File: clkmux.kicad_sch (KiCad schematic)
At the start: 9 parts, among them J7 Conn_Coaxial, U3 9DMV0141AKILF, U4 DS90C401M_NOPB

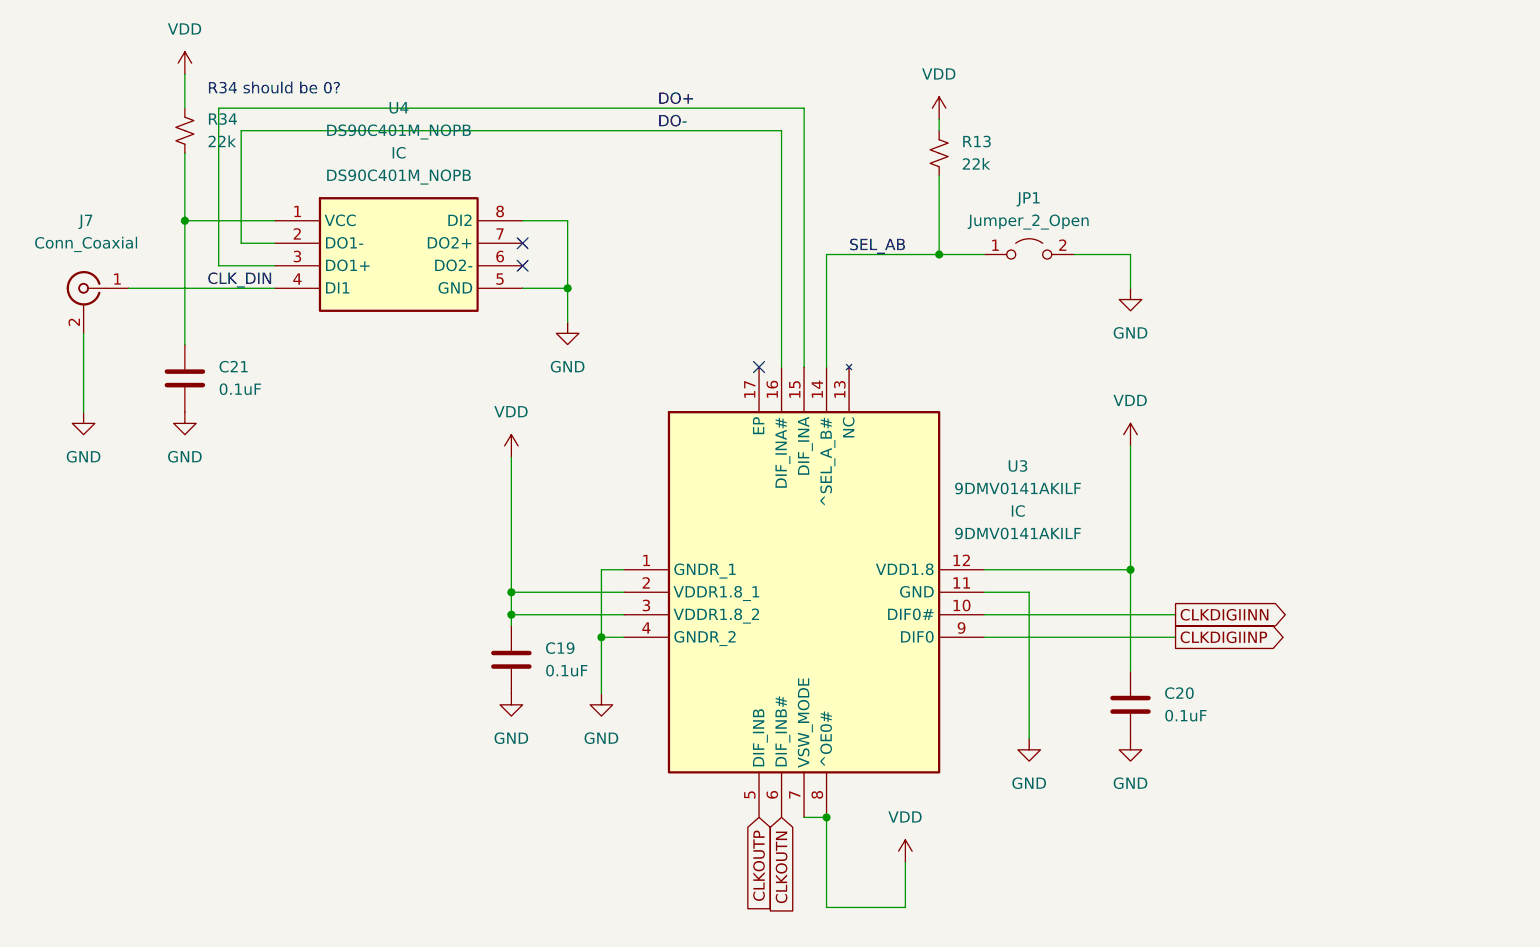
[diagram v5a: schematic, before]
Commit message: clk select related components moved to the top layer
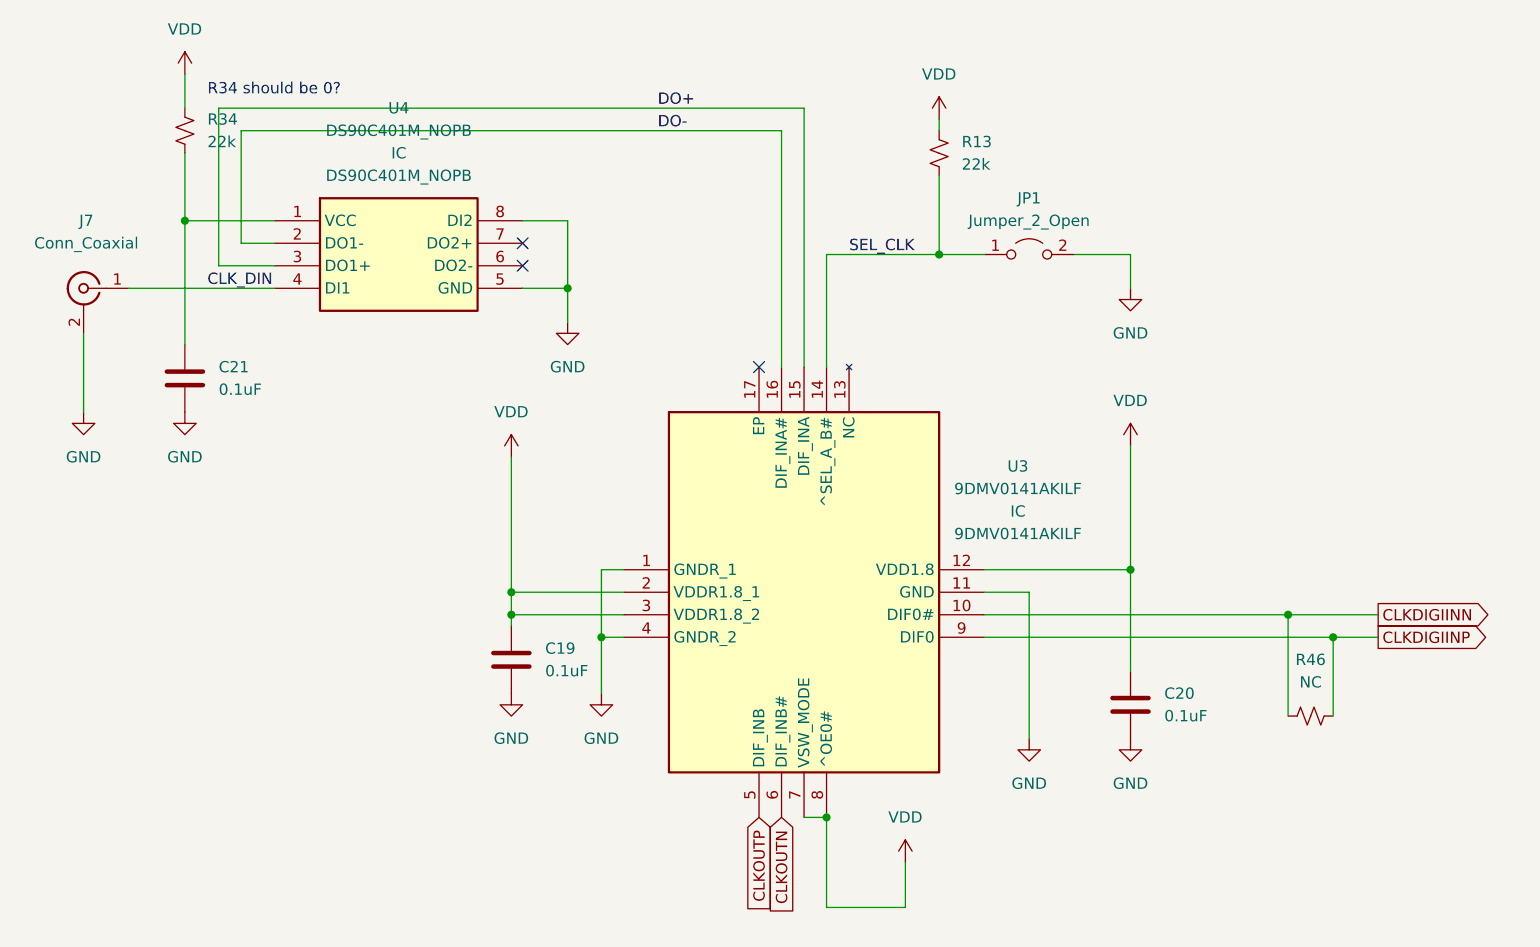
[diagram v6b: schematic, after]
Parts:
- added R46: NC, Resistor_SMD:R_0805_2012Metric_Pad1.20x1.40mm_HandSolder, symbol Device:R_Small_US
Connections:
- net CLKDIGIINN: now also R46.1
- net CLKDIGIINP: now also R46.2
- net SEL_AB renamed SEL_CLK
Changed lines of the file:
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@@
   (junction (at 71.12 72.39) (diameter 0) (color 0 0 0 0)
   )
+  (junction (at 195.58 116.84) (diameter 0) (color 0 0 0 0)
+  )
   (junction (at 156.21 76.2) (diameter 0) (color 0 0 0 0)
+  )
+  (junction (at 200.66 119.38) (diameter 0) (color 0 0 0 0)
   )
   (junction (at 177.8 111.76) (diameter 0) (color 0 0 0 0)
@@
     (stroke (width 0) (type default))
   )
+  (wire (pts (xy 200.66 119.38) (xy 161.29 119.38))
+    (stroke (width 0) (type default))
+  )
   (wire (pts (xy 177.8 111.76) (xy 177.8 123.19))
     (stroke (width 0) (type default))
@@
     (stroke (width 0) (type default))
   )
-  (wire (pts (xy 182.88 119.38) (xy 161.29 119.38))
+  (wire (pts (xy 205.74 119.38) (xy 200.66 119.38))
     (stroke (width 0) (type default))
   )
@@
     (stroke (width 0) (type default))
   )
+  (wire (pts (xy 195.58 116.84) (xy 161.29 116.84))
+    (stroke (width 0) (type default))
+  )
   (wire (pts (xy 143.51 139.7) (xy 143.51 149.86))
     (stroke (width 0) (type default))
@@
     (stroke (width 0) (type default))
   )
+  (wire (pts (xy 200.66 119.38) (xy 200.66 128.27))
+    (stroke (width 0) (type default))
+  )
   (wire (pts (xy 156.21 60.96) (xy 156.21 62.23))
     (stroke (width 0) (type default))
   )
+  (wire (pts (xy 195.58 116.84) (xy 195.58 128.27))
+    (stroke (width 0) (type default))
+  )
   (wire (pts (xy 161.29 114.3) (xy 166.37 114.3))
     (stroke (width 0) (type default))
@@
     (stroke (width 0) (type default))
   )
-  (wire (pts (xy 182.88 116.84) (xy 161.29 116.84))
+  (wire (pts (xy 205.74 116.84) (xy 195.58 116.84))
     (stroke (width 0) (type default))
   )
@@
     (effects (font (size 1.27 1.27)) (justify left bottom))
   )
-  (label "SEL_AB" (at 146.05 76.2 0) (fields_autoplaced)
+  (label "SEL_CLK" (at 146.05 76.2 0) (fields_autoplaced)
     (effects (font (size 1.27 1.27)) (justify left bottom))
   )
@@
     )
   )
-  (global_label "CLKDIGIINN" (shape output) (at 182.88 116.84 0) (fields_autoplaced)
+  (global_label "CLKDIGIINN" (shape output) (at 205.74 116.84 0) (fields_autoplaced)
     (effects (font (size 1.27 1.27)) (justify left))
-    (property "Intersheetrefs" "${INTERSHEET_REFS}" (at 195.8764 116.7606 0)
+    (property "Intersheetrefs" "${INTERSHEET_REFS}" (at 218.7364 116.7606 0)
       (effects (font (size 1.27 1.27)) (justify left) hide)
     )
@@
     )
   )
-  (global_label "CLKDIGIINP" (shape output) (at 182.88 119.38 0) (fields_autoplaced)
+  (global_label "CLKDIGIINP" (shape output) (at 205.74 119.38 0) (fields_autoplaced)
     (effects (font (size 1.27 1.27)) (justify left))
-    (property "Intersheetrefs" "${INTERSHEET_REFS}" (at 195.816 119.3006 0)
+    (property "Intersheetrefs" "${INTERSHEET_REFS}" (at 218.676 119.3006 0)
       (effects (font (size 1.27 1.27)) (justify left) hide)
     )
@@
         )
       )
+    )
+  )
+  (symbol (lib_id "Device:R_Small_US") (at 198.12 128.27 90) (unit 1)
+    (in_bom yes) (on_board yes) (dnp no) (fields_autoplaced)
+    (property "Reference" "R46" (at 198.12 121.92 90)
+      (effects (font (size 1.27 1.27)))
+    )
+    (property "Value" "NC" (at 198.12 124.46 90)
+      (effects (font (size 1.27 1.27)))
+    )
+    (property "Footprint" "Resistor_SMD:R_0805_2012Metric_Pad1.20x1.40mm_HandSolder" (at 198.12 128.27 0)
+      (effects (font (size 1.27 1.27)) hide)
+    )
+    (property "Datasheet" "~" (at 198.12 128.27 0)
+      (effects (font (size 1.27 1.27)) hide)
+    )
+    (pin "1")
+    (pin "2")
+    (instances
+      (project "qpix"
+        (path "/68db0a76-6651-4f65-9d5f-4b164c02719b/644af945-7122-4242-b9d9-3e758ef7be8c"
+          (reference "R46") (unit 1)
+        )
+      )

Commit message: lvds receiver/driver added for every endeavour port along with 3.3V power supply
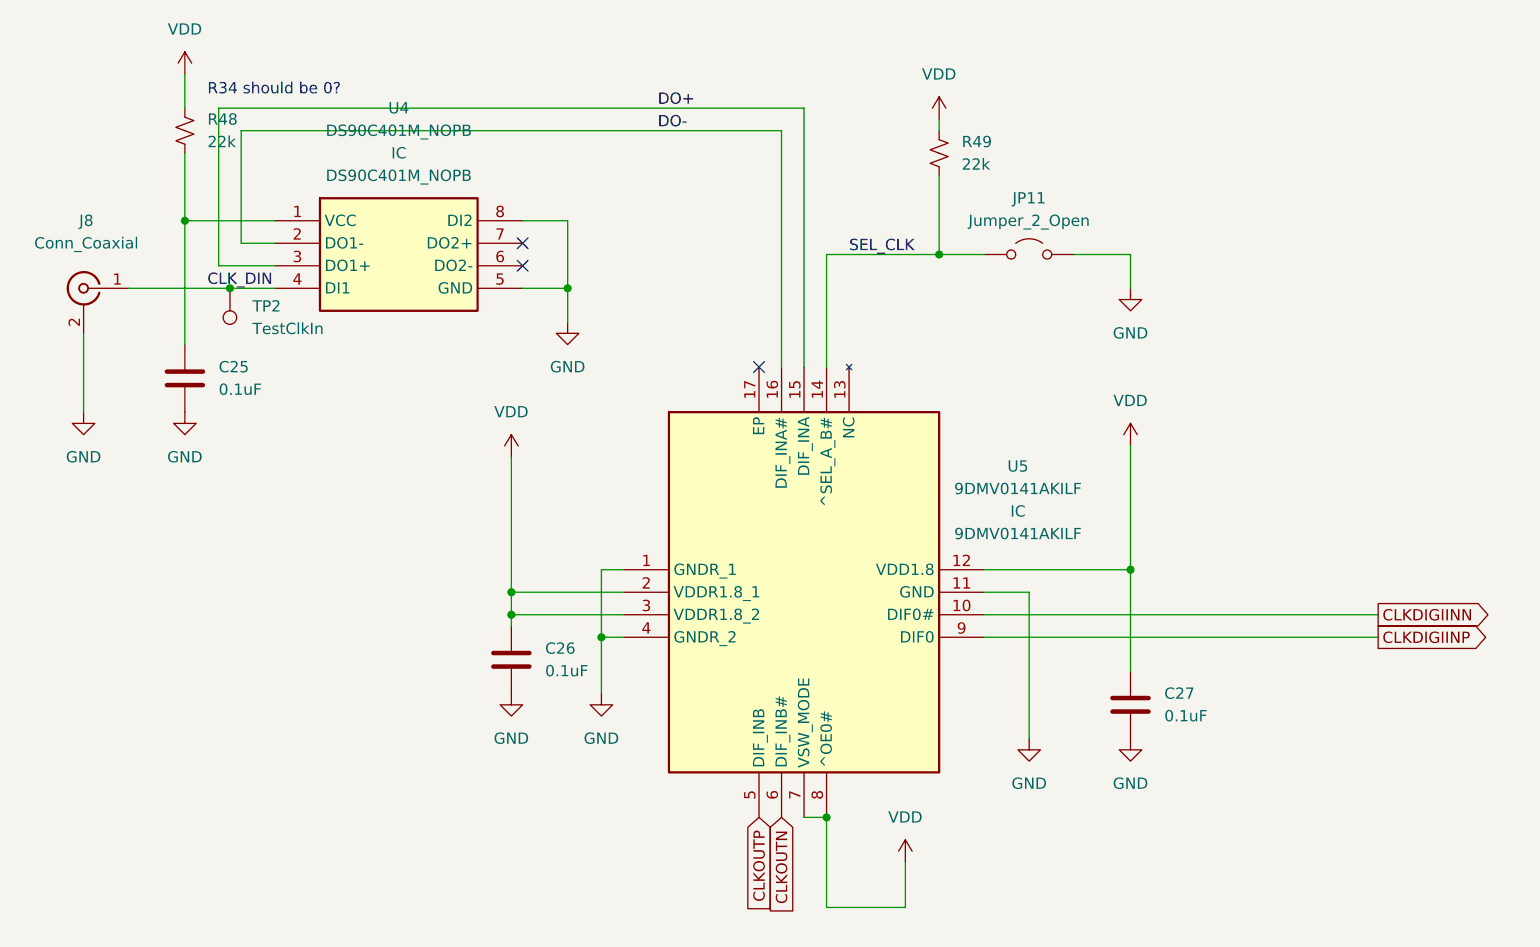
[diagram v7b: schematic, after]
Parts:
- removed R46: NC, Resistor_SMD:R_0805_2012Metric_Pad1.20x1.40mm_HandSolder, symbol Device:R_Small_US
- added TP2: TestClkIn, TestPoint:TestPoint_Loop_D3.80mm_Drill2.0mm, symbol Connector:TestPoint
- U5: renamed from U3; footprint 9DMV0141AKILF:QFN50P300X300X100-17N -> QFN50P300X300X100-17N
- renumbered C21 to C25, C19 to C26, C20 to C27, J7 to J8, JP1 to JP11, R34 to R48, R13 to R49
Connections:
- net CLK_DIN: now also TP2.1
